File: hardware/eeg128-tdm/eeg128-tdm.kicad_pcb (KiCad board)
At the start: 4 copper layers, 190 x 110 mm, 642 parts, among them J1 J1, J10 J10, J11 J11, J2 J2, J3 J3, J4 J4, J5 J5, J6 J6, J7 J7, J8 J8, J9 TYPE-C-31-M-12, U1 U1, U10 U10, U11 U11, U12 U12, U13 U13, U14 U14, U15 U15, U16 U16, U17 U17, U18 U18, U19 U19, U2 U2, U20 U20, U21 U21, U22 U22, U23 U23, U24 U24, U25 U25, U26 U26, U27 U27, U3 U3, U4 U4, U5 U5, U6 U6, U7 U7, U8 U8, U9 U9, Y1 Y1

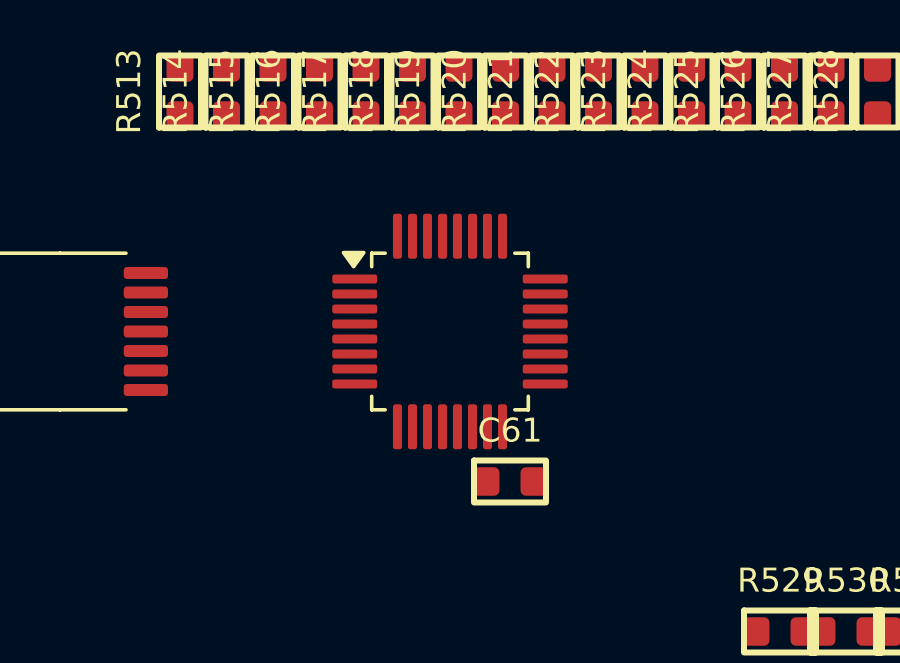
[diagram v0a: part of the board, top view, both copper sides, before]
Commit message: Materialize generated KiCad schematic and release manifest
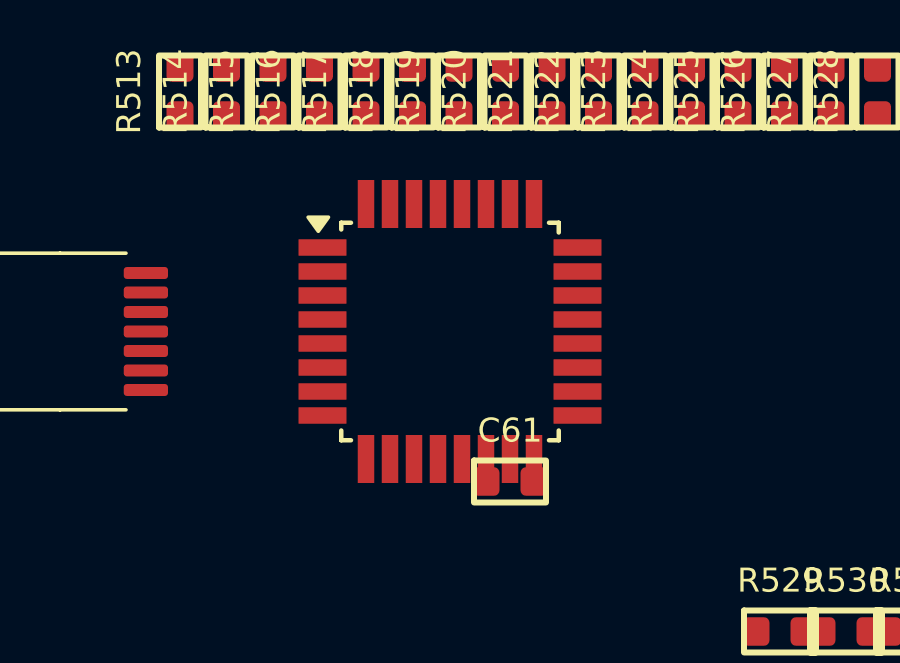
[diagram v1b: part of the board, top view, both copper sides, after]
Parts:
- U21: footprint LQFP-32_5x5mm_P0.5mm -> TQFP-32_7x7mm_P0.8mm

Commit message: Materialize generated KiCad schematic and release manifest
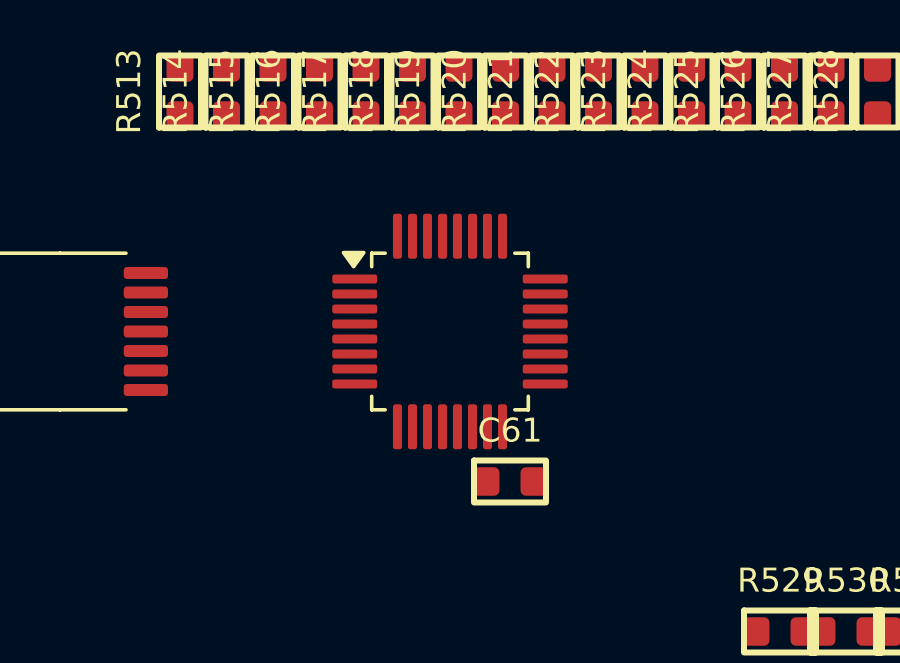
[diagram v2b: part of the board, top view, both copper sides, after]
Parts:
- U21: footprint TQFP-32_7x7mm_P0.8mm -> LQFP-32_5x5mm_P0.5mm

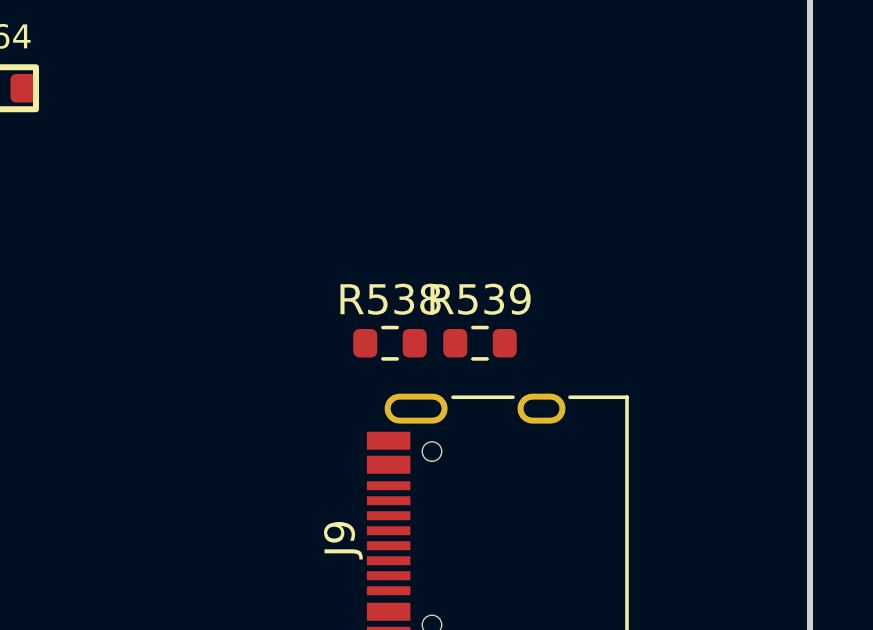
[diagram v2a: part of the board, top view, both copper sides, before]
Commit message: Materialize generated KiCad schematic and release manifest
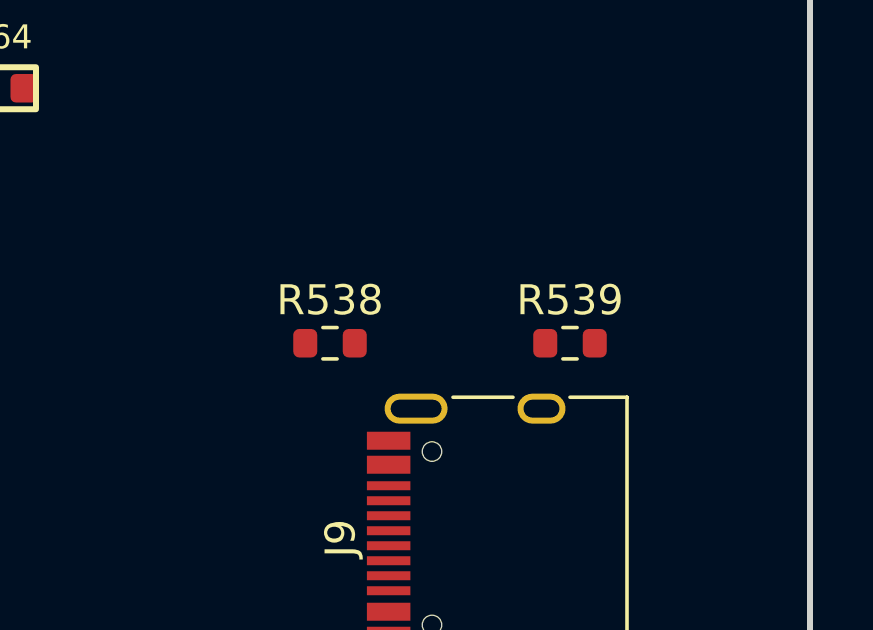
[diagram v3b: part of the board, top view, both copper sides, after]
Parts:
- moved R539 3.00 mm to (187.0, 70.5)
- moved R538 2.00 mm to (179.0, 70.5)
